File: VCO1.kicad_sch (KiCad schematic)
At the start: 62 parts, among them Q7 MMBT3904-7-F, Q8 MMBT3904-7-F, Q9 MMBF4391LT1G, SW3 SW_SPDT, SW4 SW_SPDT, SW5 SYNC, U3 TL072, U4 TL072, U5 TL072

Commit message: more work...
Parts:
- C11, C12, C13, C14: footprint Capacitor_SMD:C_0805_2012Metric_Pad1.18x1.45mm_HandSolder -> Capacitor_SMD:C_0805_2012Metric
- C15, C16, C18, C19, C20, C22: footprint Capacitor_SMD:C_0805_2012Metric_Pad1.18x1.45mm_HandSolder -> Capacitor_SMD:C_0603_1608Metric
- C17, C21: value 1n -> 1nF; footprint Capacitor_SMD:C_0805_2012Metric_Pad1.18x1.45mm_HandSolder -> Capacitor_SMD:C_0603_1608Metric
- R30, R31, R32, R33, R34, R35, R36, R37, R38, R39, R40, R41, R42, R43, R44, R45, R46, R47, R48, R49, R50, R51, R52, R53, R54, R55, R56, R57, R58, R59, R60, R61, R62, R63: footprint Resistor_SMD:R_0805_2012Metric_Pad1.20x1.40mm_HandSolder -> Resistor_SMD:R_0603_1608Metric
- RV10: footprint Potentiometer_THT:Potentiometer_Alps_RK09K_Single_Vertical -> Potentiometer_SMD:Potentiometer_Bourns_TC33X_Vertical

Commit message: finishing schematic 1.0
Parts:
- RV11: footprint Potentiometer_THT:Potentiometer_Alps_RK09K_Single_Vertical -> Potentiometer_SMD:Potentiometer_Bourns_TC33X_Vertical
- SW3, SW4, SW5: footprint SynthProjConnectors:ST-0-102-A01-T000-LF -> SynthProjConnectors:MTS-103-A01-T0
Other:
- note added: "1V/Oct Scale Trim"
- note added: "Pulse Width"

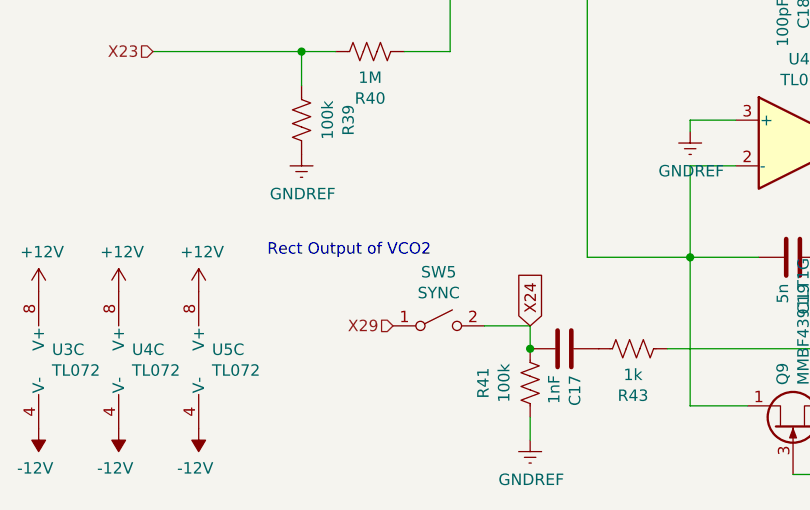
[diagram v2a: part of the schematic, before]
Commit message: doing some routing - split sequencer into another project
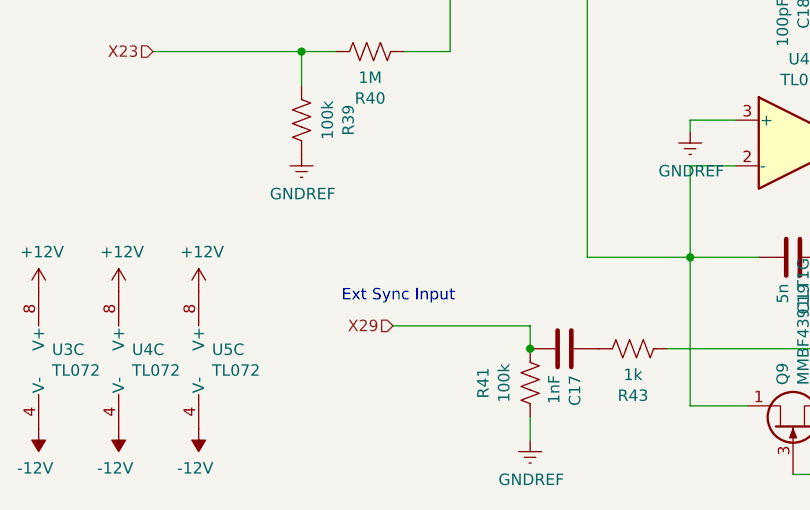
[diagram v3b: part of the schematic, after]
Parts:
- removed SW5: SYNC, SynthProjConnectors:MTS-103-A01-T0, symbol Switch:SW_SPST
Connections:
- net X24 is gone; now on net X29: C17.2, R41.1
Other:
- note added: "Ext Sync Input"
- note removed: "Rect Output of VCO2"
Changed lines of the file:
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@@
-    (stroke (width 0) (type default))
-  )
-  (wire (pts (xy 135.89 137.16) (xy 130.81 137.16))
     (stroke (width 0) (type default))
   )
@@
     (stroke (width 0) (type default))
   )
+  (wire (pts (xy 120.65 137.16) (xy 135.89 137.16))
+    (stroke (width 0) (type default))
+  )
   (wire (pts (xy 116.84 53.34) (xy 113.03 53.34))
     (stroke (width 0) (type default))
@@
     (effects (font (size 1.27 1.27)) (justify left bottom))
   )
-  (text "Rect Output of VCO2" (at 106.68 129.54 0)
+  (text "Ext Sync Input" (at 114.935 134.62 0)
     (effects (font (size 1.27 1.27)) (justify left bottom))
   )
@@
     (property "Intersheetrefs" "${INTERSHEET_REFS}" (at 69.5863 58.42 0)
       (effects (font (size 1.27 1.27)) (justify right) hide)
-    )
-  )
-  (global_label "X24" (shape input) (at 135.89 137.16 90) (fields_autoplaced)
-    (effects (font (size 1.27 1.27)) (justify left))
-    (property "Intersheetrefs" "${INTERSHEET_REFS}" (at 135.89 130.5463 90)
-      (effects (font (size 1.27 1.27)) (justify left) hide)
     )
   )
@@
         )
       )
-    )
-  )
-  (symbol (lib_id "Switch:SW_SPST") (at 125.73 137.16 0) (unit 1)
-    (in_bom yes) (on_board yes) (dnp no)
-    (property "Reference" "SW5" (at 125.73 131.191 0)
-      (effects (font (size 1.27 1.27)))
-    )
-    (property "Value" "SYNC" (at 125.73 133.5024 0)
-      (effects (font (size 1.27 1.27)))
-    )
-    (property "Footprint" "SynthProjConnectors:MTS-103-A01-T0" (at 125.73 137.16 0)
-      (effects (font (size 1.27 1.27)) hide)
-    )
-    (property "Datasheet" "~" (at 125.73 137.16 0)
-      (effects (font (size 1.27 1.27)) hide)
-    )
-    (pin "1")
-    (pin "2")
-    (instances
-      (project "SynthProj"
-        (path "/9021c97e-351f-4ed9-b393-50257df6a463/00000000-0000-0000-0000-0000659d0967"
-          (reference "SW5") (unit 1)
-        )
-      )

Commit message: lots of routes, added vco3, lfo2.
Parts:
- SW3, SW4: footprint SynthProjConnectors:MTS-103-A01-T0 -> SynthProjConnectors:SMTS-102
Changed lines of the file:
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@@
       (effects (font (size 1.27 1.27)))
     )
-    (property "Footprint" "SynthProjConnectors:MTS-103-A01-T0" (at 58.42 101.6 0)
+    (property "Footprint" "SynthProjConnectors:SMTS-102" (at 58.42 101.6 0)
       (effects (font (size 1.27 1.27)) hide)
     )
@@
       (effects (font (size 1.27 1.27)))
     )
-    (property "Footprint" "SynthProjConnectors:MTS-103-A01-T0" (at 58.42 110.49 0)
+    (property "Footprint" "SynthProjConnectors:SMTS-102" (at 58.42 110.49 0)
       (effects (font (size 1.27 1.27)) hide)
     )

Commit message: more and more and more and more and more routing
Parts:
- removed C11, C12: 4.7uF, Capacitor_SMD:C_0805_2012Metric, symbol Device:C
- removed C15, C16: 47nF, Capacitor_SMD:C_0603_1608Metric, symbol Device:C
- added C2, C3, C6, C7: 470nF, Capacitor_SMD:C_0805_2012Metric, symbol Device:C
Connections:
- net +12V: now also C2.2, C3.2
- net -12V: now also C6.1, C7.1
- net GNDREF: now also C2.1, C3.1, C6.2, C7.2
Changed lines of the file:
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@@
   (junction (at 170.18 63.5) (diameter 0) (color 0 0 0 0)
   )
-  (junction (at 53.34 148.59) (diameter 0) (color 0 0 0 0)
-  )
   (junction (at 57.15 33.02) (diameter 0) (color 0 0 0 0)
   )
@@
   (junction (at 215.9 130.81) (diameter 0) (color 0 0 0 0)
   )
+  (junction (at 53.34 140.97) (diameter 0) (color 0 0 0 0)
+  )
   (junction (at 186.69 139.7) (diameter 0) (color 0 0 0 0)
   )
@@
   (junction (at 226.06 93.98) (diameter 0) (color 0 0 0 0)
   )
+  (junction (at 53.34 148.59) (diameter 0) (color 0 0 0 0)
+  )
   (junction (at 226.06 85.09) (diameter 0) (color 0 0 0 0)
   )
@@
   (junction (at 142.24 63.5) (diameter 0) (color 0 0 0 0)
   )
-  (junction (at 66.04 140.97) (diameter 0) (color 0 0 0 0)
-  )
   (junction (at 127 86.36) (diameter 0) (color 0 0 0 0)
   )
+  (junction (at 66.04 140.97) (diameter 0) (color 0 0 0 0)
+  )
   (junction (at 200.66 66.04) (diameter 0) (color 0 0 0 0)
   )
@@
   (junction (at 59.69 133.35) (diameter 0) (color 0 0 0 0)
   )
-  (junction (at 53.34 140.97) (diameter 0) (color 0 0 0 0)
-  )
   (junction (at 59.69 148.59) (diameter 0) (color 0 0 0 0)
   )
@@
     (stroke (width 0) (type default))
   )
+  (wire (pts (xy 53.34 140.97) (xy 59.69 140.97))
+    (stroke (width 0) (type default))
+  )
   (wire (pts (xy 231.14 130.81) (xy 231.14 134.62))
     (stroke (width 0) (type default))
@@
     (stroke (width 0) (type default))
   )
-  (wire (pts (xy 53.34 140.97) (xy 59.69 140.97))
-    (stroke (width 0) (type default))
-  )
   (wire (pts (xy 223.52 53.34) (xy 226.06 53.34))
     (stroke (width 0) (type default))
@@
     )
   )
-  (symbol (lib_id "Device:C") (at 53.34 137.16 180) (unit 1)
-    (in_bom yes) (on_board yes) (dnp no)
-    (property "Reference" "C11" (at 59.7408 137.16 90)
-      (effects (font (size 1.27 1.27)))
-    )
-    (property "Value" "4.7uF" (at 57.4294 137.16 90)
-      (effects (font (size 1.27 1.27)))
-    )
-    (property "Footprint" "Capacitor_SMD:C_0805_2012Metric" (at 52.3748 133.35 0)
-      (effects (font (size 1.27 1.27)) hide)
-    )
-    (property "Datasheet" "~" (at 53.34 137.16 0)
-      (effects (font (size 1.27 1.27)) hide)
-    )
-    (pin "1")
-    (pin "2")
-    (instances
-      (project "SynthProj"
-        (path "/9021c97e-351f-4ed9-b393-50257df6a463/00000000-0000-0000-0000-0000659d0967"
-          (reference "C11") (unit 1)
-        )
-        (path "/9021c97e-351f-4ed9-b393-50257df6a463/00000000-0000-0000-0000-0000659a4e2e"
-          (reference "C?") (unit 1)
-        )
-      )
-    )
-  )
   (symbol (lib_id "Device:C") (at 59.69 137.16 180) (unit 1)
     (in_bom yes) (on_board yes) (dnp no)
@@
     )
   )
-  (symbol (lib_id "Device:C") (at 66.04 137.16 180) (unit 1)
-    (in_bom yes) (on_board yes) (dnp no)
-    (property "Reference" "C15" (at 72.4408 137.16 90)
-      (effects (font (size 1.27 1.27)))
-    )
-    (property "Value" "47nF" (at 70.1294 137.16 90)
-      (effects (font (size 1.27 1.27)))
-    )
-    (property "Footprint" "Capacitor_SMD:C_0603_1608Metric" (at 65.0748 133.35 0)
-      (effects (font (size 1.27 1.27)) hide)
-    )
-    (property "Datasheet" "~" (at 66.04 137.16 0)
-      (effects (font (size 1.27 1.27)) hide)
-    )
-    (pin "2")
-    (pin "1")
-    (instances
-      (project "SynthProj"
-        (path "/9021c97e-351f-4ed9-b393-50257df6a463/00000000-0000-0000-0000-0000659d0967"
-          (reference "C15") (unit 1)
-        )
-        (path "/9021c97e-351f-4ed9-b393-50257df6a463/00000000-0000-0000-0000-0000659a4e2e"
-          (reference "C?") (unit 1)
-        )
-      )
-    )
-  )
-  (symbol (lib_id "Device:C") (at 53.34 144.78 180) (unit 1)
-    (in_bom yes) (on_board yes) (dnp no)
-    (property "Reference" "C12" (at 59.7408 144.78 90)
-      (effects (font (size 1.27 1.27)))
-    )
-    (property "Value" "4.7uF" (at 57.4294 144.78 90)
-      (effects (font (size 1.27 1.27)))
-    )
-    (property "Footprint" "Capacitor_SMD:C_0805_2012Metric" (at 52.3748 140.97 0)
-      (effects (font (size 1.27 1.27)) hide)
-    )
-    (property "Datasheet" "~" (at 53.34 144.78 0)
-      (effects (font (size 1.27 1.27)) hide)
-    )
-    (pin "1")
-    (pin "2")
-    (instances
-      (project "SynthProj"
-        (path "/9021c97e-351f-4ed9-b393-50257df6a463/00000000-0000-0000-0000-0000659d0967"
-          (reference "C12") (unit 1)
-        )
-        (path "/9021c97e-351f-4ed9-b393-50257df6a463/00000000-0000-0000-0000-0000659a4e2e"
-          (reference "C?") (unit 1)
-        )
-      )
-    )
-  )
   (symbol (lib_id "Device:C") (at 59.69 144.78 180) (unit 1)
     (in_bom yes) (on_board yes) (dnp no)
     (property "Reference" "C14" (at 66.0908 144.78 90)
-      (effects (font (size 1.27 1.27)))
+      (effects (font (size 1.27 1.27)) hide)
     )
     (property "Value" "470nF" (at 63.7794 144.78 90)
@@
     )
   )
-  (symbol (lib_id "Device:C") (at 66.04 144.78 180) (unit 1)
-    (in_bom yes) (on_board yes) (dnp no)
-    (property "Reference" "C16" (at 72.4408 144.78 90)
-      (effects (font (size 1.27 1.27)))
-    )
-    (property "Value" "47nF" (at 70.1294 144.78 90)
-      (effects (font (size 1.27 1.27)))
-    )
-    (property "Footprint" "Capacitor_SMD:C_0603_1608Metric" (at 65.0748 140.97 0)
-      (effects (font (size 1.27 1.27)) hide)
-    )
-    (property "Datasheet" "~" (at 66.04 144.78 0)
-      (effects (font (size 1.27 1.27)) hide)
-    )
-    (pin "1")
-    (pin "2")
-    (instances
-      (project "SynthProj"
-        (path "/9021c97e-351f-4ed9-b393-50257df6a463/00000000-0000-0000-0000-0000659d0967"
-          (reference "C16") (unit 1)
-        )
-        (path "/9021c97e-351f-4ed9-b393-50257df6a463/00000000-0000-0000-0000-0000659a4e2e"
-          (reference "C?") (unit 1)
-        )
-      )
-    )
-  )
   (symbol (lib_id "Amplifier_Operational:TL072") (at 88.9 69.85 0) (unit 1)
     (in_bom yes) (on_board yes) (dnp no)
@@
         )
       )
+    )
+  )
+  (symbol (lib_id "Device:C") (at 53.34 144.78 180) (unit 1)
+    (in_bom yes) (on_board yes) (dnp no)
+    (property "Reference" "C6" (at 59.7408 144.78 90)
+      (effects (font (size 1.27 1.27)))
+    )
+    (property "Value" "470nF" (at 57.4294 144.78 90)
+      (effects (font (size 1.27 1.27)))
+    )
+    (property "Footprint" "Capacitor_SMD:C_0805_2012Metric" (at 52.3748 140.97 0)
+      (effects (font (size 1.27 1.27)) hide)
+    )
+    (property "Datasheet" "~" (at 53.34 144.78 0)
+      (effects (font (size 1.27 1.27)) hide)
+    )
+    (pin "1")
+    (pin "2")
+    (instances
+      (project "SynthProj"
+        (path "/9021c97e-351f-4ed9-b393-50257df6a463/00000000-0000-0000-0000-0000659d0967"
+          (reference "C6") (unit 1)
+        )
+        (path "/9021c97e-351f-4ed9-b393-50257df6a463/00000000-0000-0000-0000-0000659a4e2e"
+          (reference "C?") (unit 1)
+        )
+      )
+    )
+  )
+  (symbol (lib_id "Device:C") (at 66.04 137.16 180) (unit 1)
+    (in_bom yes) (on_board yes) (dnp no)
+    (property "Reference" "C2" (at 72.4408 137.16 90)
+      (effects (font (size 1.27 1.27)))
+    )
+    (property "Value" "470nF" (at 70.1294 137.16 90)
+      (effects (font (size 1.27 1.27)))
+    )
+    (property "Footprint" "Capacitor_SMD:C_0805_2012Metric" (at 65.0748 133.35 0)
+      (effects (font (size 1.27 1.27)) hide)
+    )
+    (property "Datasheet" "~" (at 66.04 137.16 0)
+      (effects (font (size 1.27 1.27)) hide)
+    )
+    (pin "1")
+    (pin "2")
+    (instances
+      (project "SynthProj"
+        (path "/9021c97e-351f-4ed9-b393-50257df6a463/00000000-0000-0000-0000-0000659d0967"
+          (reference "C2") (unit 1)
+        )
+        (path "/9021c97e-351f-4ed9-b393-50257df6a463/00000000-0000-0000-0000-0000659a4e2e"
+          (reference "C?") (unit 1)
+        )
+      )
+    )
+  )
+  (symbol (lib_id "Device:C") (at 66.04 144.78 180) (unit 1)
+    (in_bom yes) (on_board yes) (dnp no)
+    (property "Reference" "C7" (at 72.4408 144.78 90)
+      (effects (font (size 1.27 1.27)))
+    )
+    (property "Value" "470nF" (at 70.1294 144.78 90)
+      (effects (font (size 1.27 1.27)))
+    )
+    (property "Footprint" "Capacitor_SMD:C_0805_2012Metric" (at 65.0748 140.97 0)
+      (effects (font (size 1.27 1.27)) hide)
+    )
+    (property "Datasheet" "~" (at 66.04 144.78 0)
+      (effects (font (size 1.27 1.27)) hide)
+    )
+    (pin "1")
+    (pin "2")
+    (instances
+      (project "SynthProj"
+        (path "/9021c97e-351f-4ed9-b393-50257df6a463/00000000-0000-0000-0000-0000659d0967"
+          (reference "C7") (unit 1)
+        )
+        (path "/9021c97e-351f-4ed9-b393-50257df6a463/00000000-0000-0000-0000-0000659a4e2e"
+          (reference "C?") (unit 1)
+        )
+      )
+    )
+  )
+  (symbol (lib_id "Device:C") (at 53.34 137.16 180) (unit 1)
+    (in_bom yes) (on_board yes) (dnp no)
+    (property "Reference" "C3" (at 59.7408 137.16 90)
+      (effects (font (size 1.27 1.27)))
+    )
+    (property "Value" "470nF" (at 57.4294 137.16 90)
+      (effects (font (size 1.27 1.27)))
+    )
+    (property "Footprint" "Capacitor_SMD:C_0805_2012Metric" (at 52.3748 133.35 0)
+      (effects (font (size 1.27 1.27)) hide)
+    )
+    (property "Datasheet" "~" (at 53.34 137.16 0)
+      (effects (font (size 1.27 1.27)) hide)
+    )
+    (pin "1")
+    (pin "2")
+    (instances
+      (project "SynthProj"
+        (path "/9021c97e-351f-4ed9-b393-50257df6a463/00000000-0000-0000-0000-0000659d0967"
+          (reference "C3") (unit 1)
+        )
+        (path "/9021c97e-351f-4ed9-b393-50257df6a463/00000000-0000-0000-0000-0000659a4e2e"
+          (reference "C?") (unit 1)
+        )
+      )

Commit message: created manufacturing files
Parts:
- RV12, RV8, RV9: value 100k -> 50k
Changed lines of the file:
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@@
       (effects (font (size 1.27 1.27)) (justify right))
     )
-    (property "Value" "100k" (at 75.057 49.0982 0)
+    (property "Value" "50k" (at 75.057 49.0982 0)
       (effects (font (size 1.27 1.27)) (justify right))
     )
@@
       (effects (font (size 1.27 1.27)) (justify right))
     )
-    (property "Value" "100k" (at 76.327 31.3182 0)
+    (property "Value" "50k" (at 76.327 31.3182 0)
       (effects (font (size 1.27 1.27)) (justify right))
     )
@@
       (effects (font (size 1.27 1.27)) (justify right))
     )
-    (property "Value" "100k" (at 242.443 127.4318 0)
+    (property "Value" "50k" (at 242.443 127.4318 0)
       (effects (font (size 1.27 1.27)) (justify right))
     )
